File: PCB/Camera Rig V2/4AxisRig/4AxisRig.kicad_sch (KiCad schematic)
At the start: 1 part

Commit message: PCB V2 first draft
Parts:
- added H1, H2, H3, H4: MountingHole, MountingHole:MountingHole_3.2mm_M3, symbol Mechanical:MountingHole
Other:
- sheet MCU ESP32 ports: added EN_DRIVERS; removed EN
- sheet USB Power ports: added USB_CC1, USB_CC2; removed none

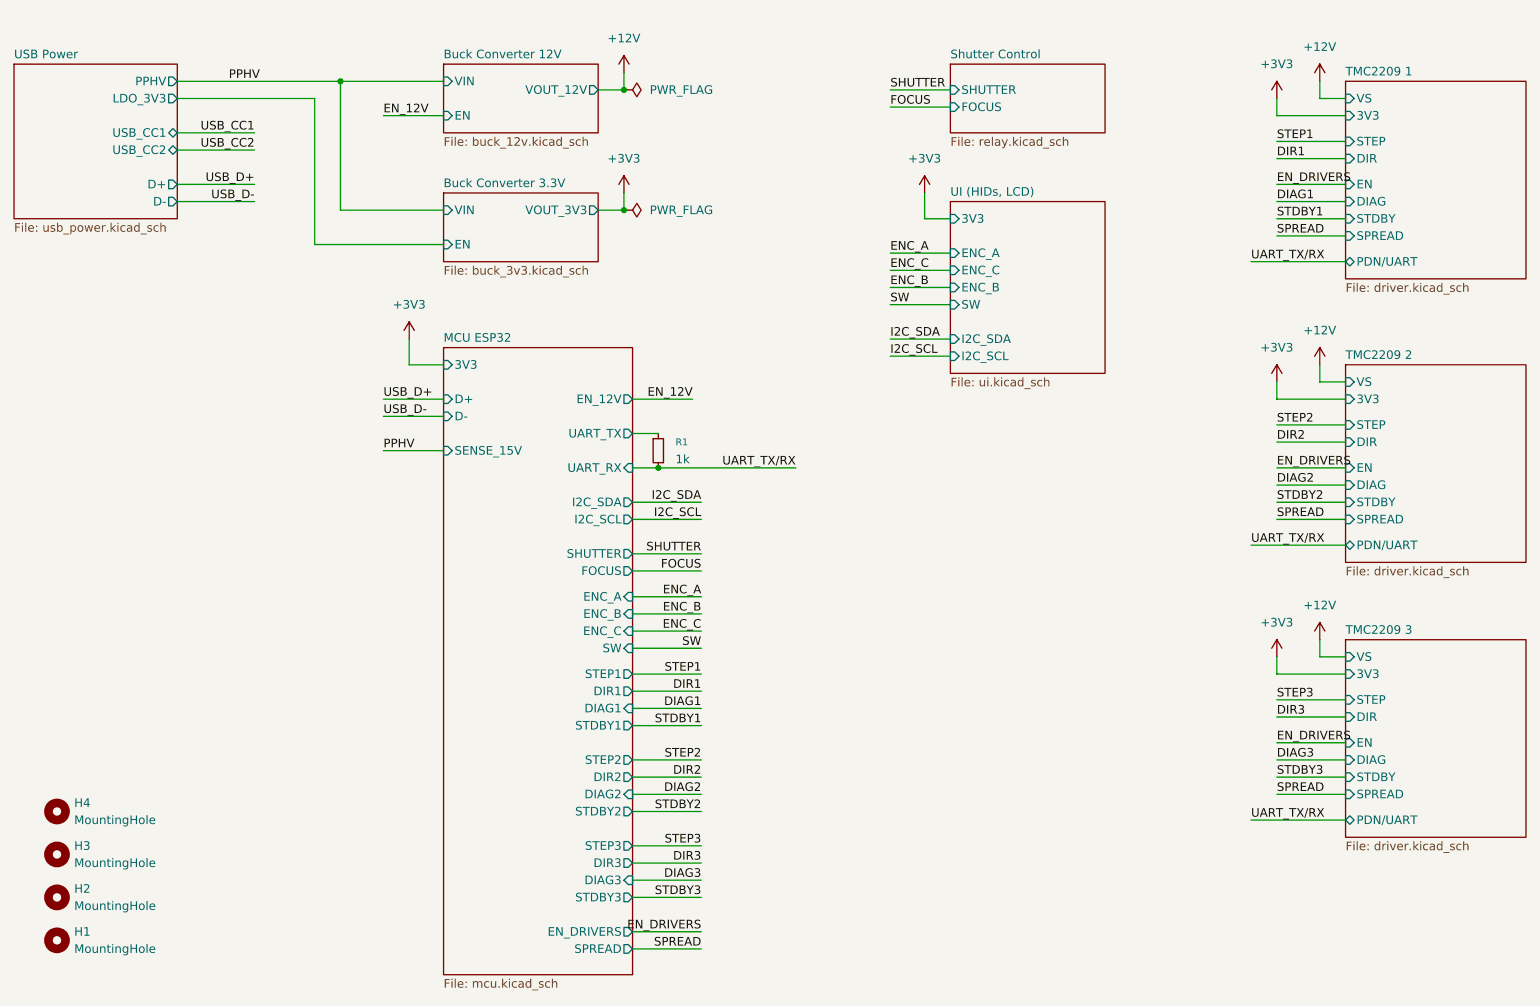
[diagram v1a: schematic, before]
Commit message: Netclass Improvements
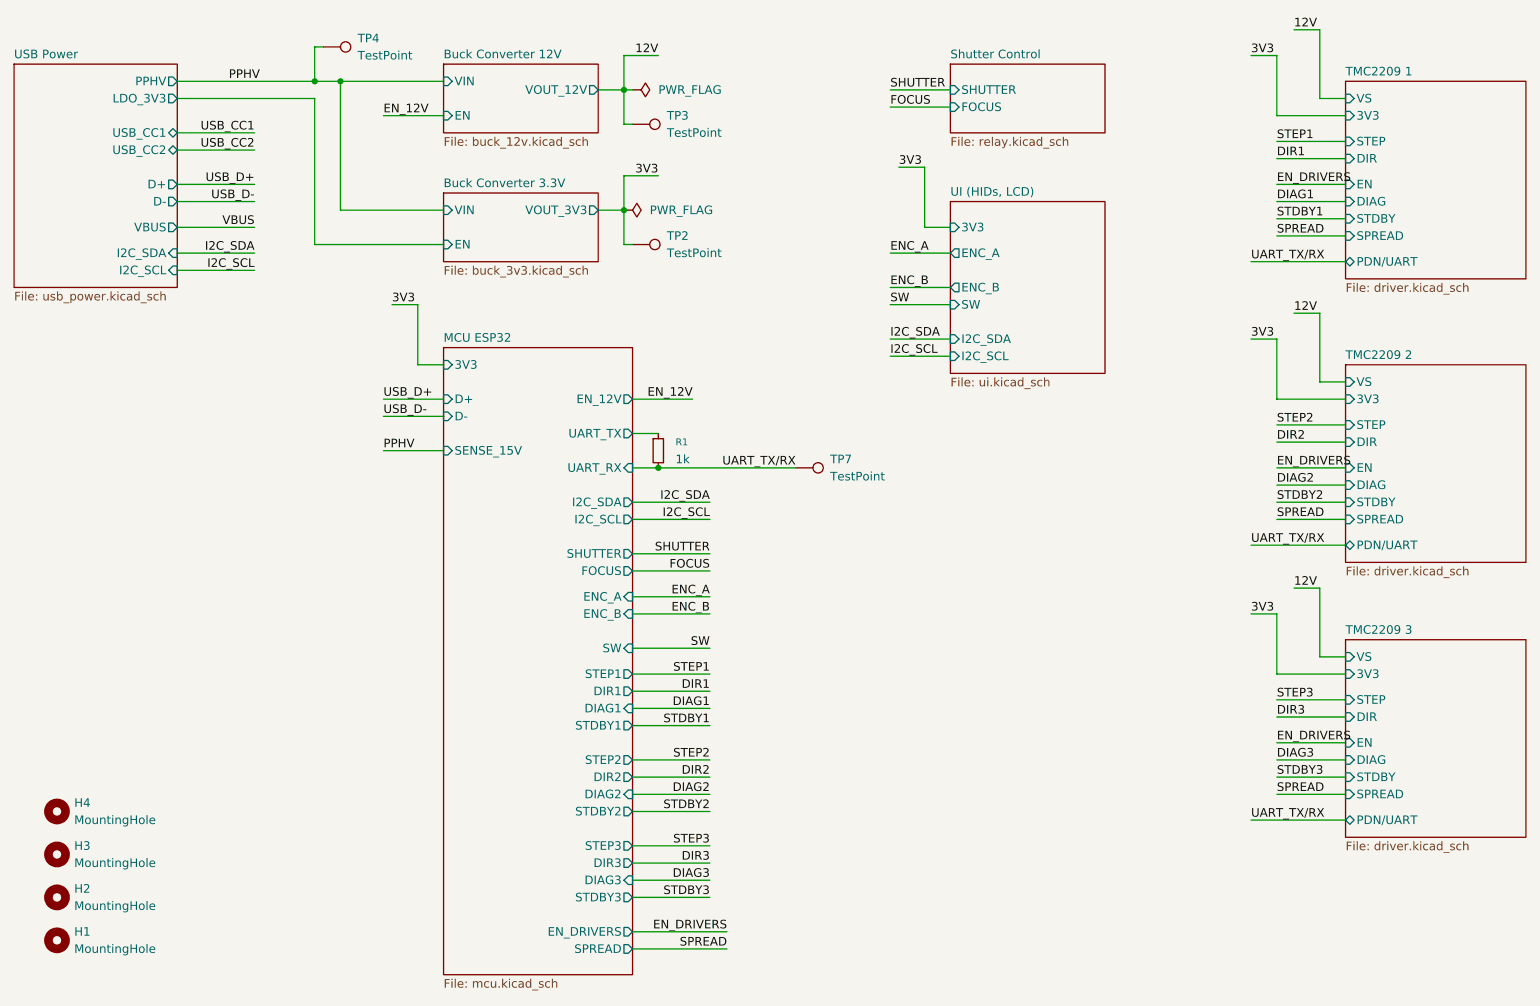
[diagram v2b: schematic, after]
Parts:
- added TP2, TP3, TP4: TestPoint, TestPoint:TestPoint_Pad_1.0x1.0mm, symbol Connector:TestPoint
- added TP7: TestPoint, TestPoint:TestPoint_Keystone_5000-5004_Miniature, symbol Connector:TestPoint
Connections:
- net PPHV: now also TP4.1
- net UART_TX/RX: now also TP7.1
- new net 12V: TP3.1
- new net 3V3: TP2.1
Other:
- sheet MCU ESP32 ports: added none; removed ENC_C
- sheet UI (HIDs, LCD) ports: added none; removed ENC_C
- sheet USB Power ports: added I2C_SCL, I2C_SDA, VBUS; removed none
